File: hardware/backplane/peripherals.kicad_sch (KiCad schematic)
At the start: 0 parts

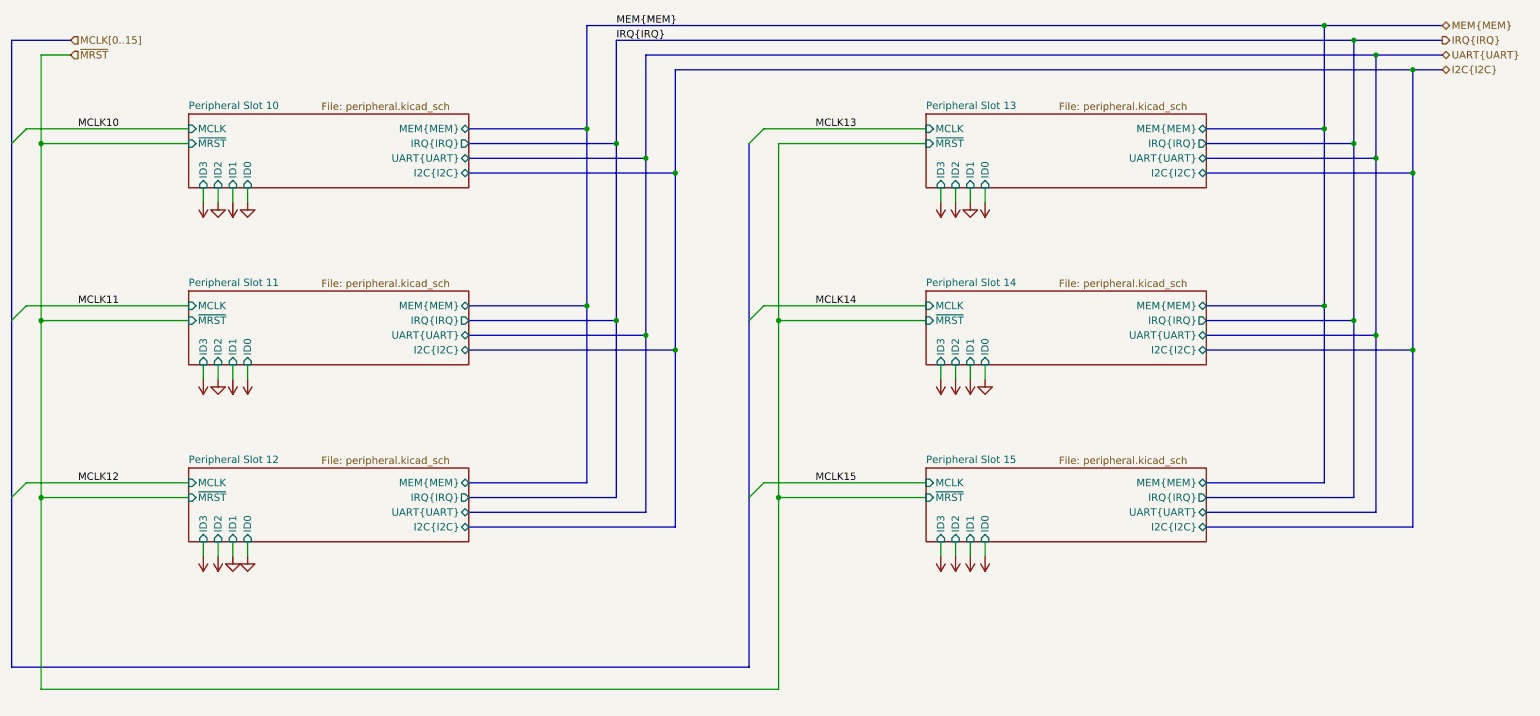
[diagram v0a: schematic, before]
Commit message: feat: Re-add peripheral MCLK, add to memory lines (#3)
Need MCLK to maintain peripheral synchronization.  Add missing memory
access size and latch lines.
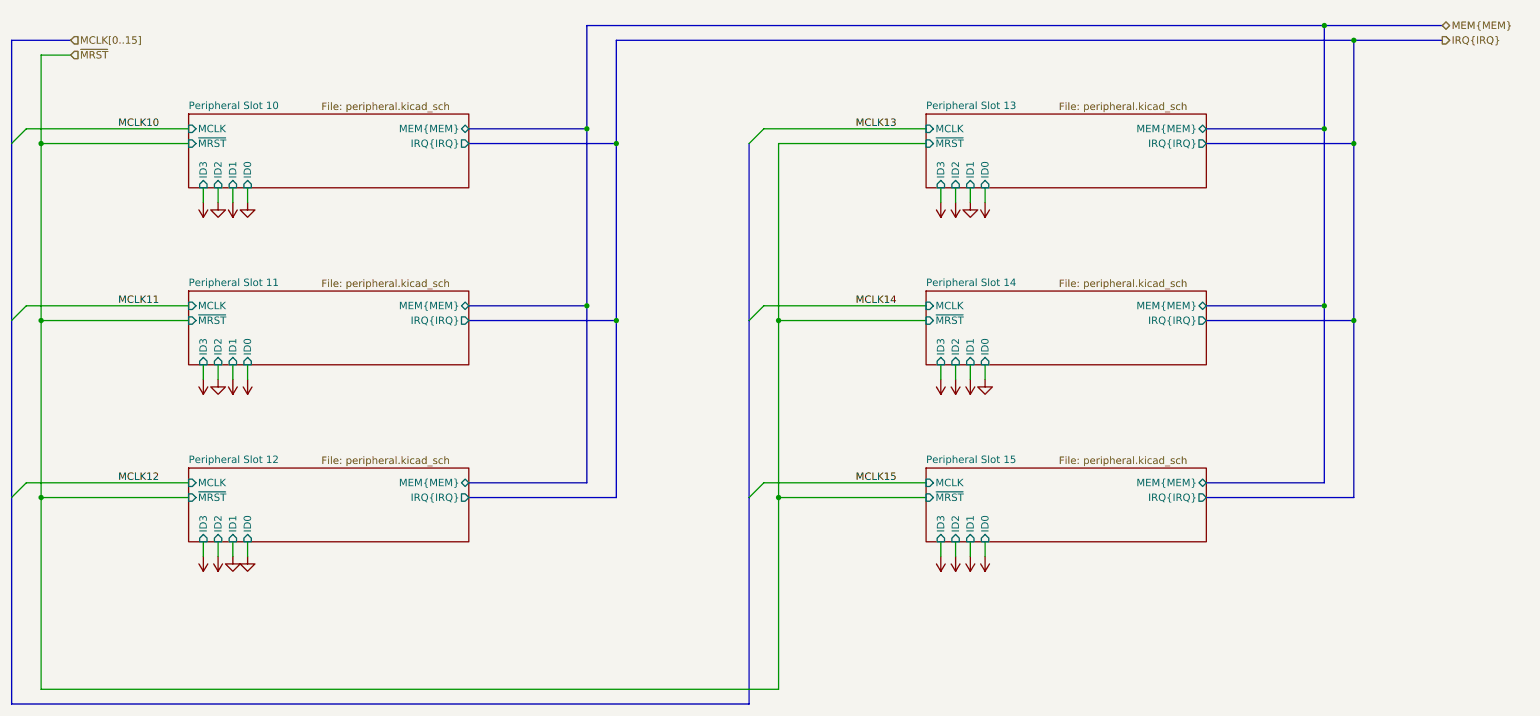
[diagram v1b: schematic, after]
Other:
- sheet Peripheral Slot 10 ports: added none; removed I2C{I2C}, UART{UART}
- sheet Peripheral Slot 11 ports: added none; removed I2C{I2C}, UART{UART}
- sheet Peripheral Slot 12 ports: added none; removed I2C{I2C}, UART{UART}
- sheet Peripheral Slot 13 ports: added none; removed I2C{I2C}, UART{UART}
- sheet Peripheral Slot 14 ports: added none; removed I2C{I2C}, UART{UART}
- sheet Peripheral Slot 15 ports: added none; removed I2C{I2C}, UART{UART}
